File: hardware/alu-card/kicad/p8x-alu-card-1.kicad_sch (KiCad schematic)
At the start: 9 parts, among them U1 74HCT377, U2 74HCT244, U3 74HCT377, U4 74HCT244, U5 74HCT377, U6 74HCT244, U7 74HCT377, U8 74HCT244, U9 74HCT181

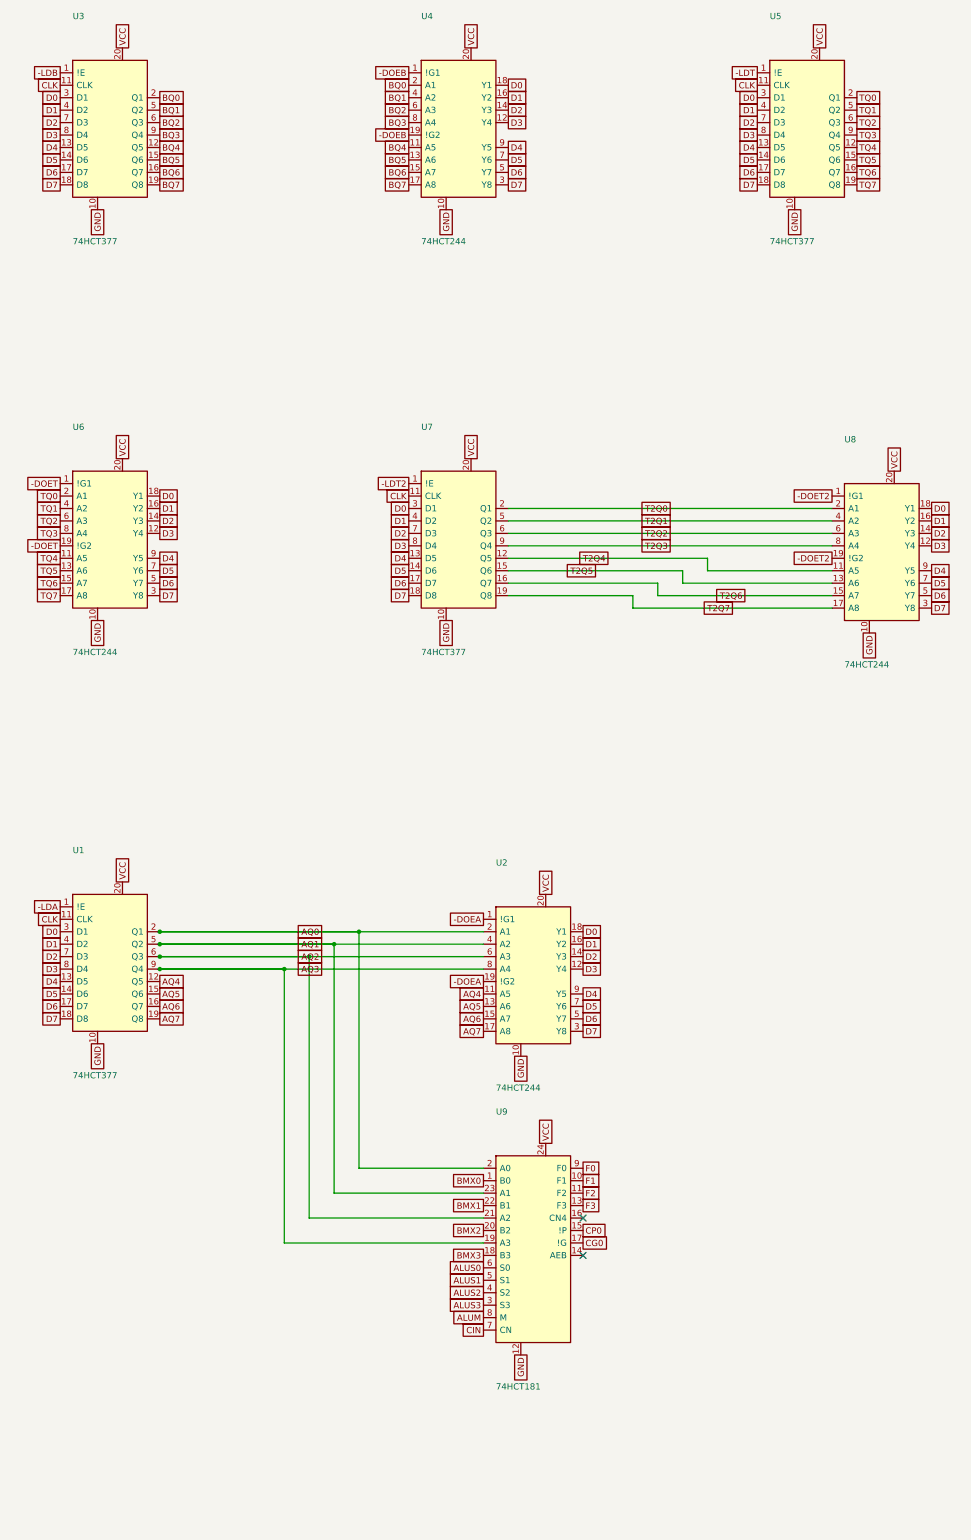
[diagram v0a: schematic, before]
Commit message: feat(sch): draw every P8X card schematic by function
Extend the functional-sheet grouping from the io-card to the control,
regbank, alu, memory, cf, ps2 and bustest cards. functional_sheets now
attaches unnamed glue gates, LEDs, resistors and connectors to the block
they share the most local nets with, so each block lists only its main
parts. A net with two or more pins on a sheet is now wired there even if
it continues elsewhere (its global name label rides on the wire), and
every wire is oriented by drawing side. The regbank gets one pointer per
sheet; the ps2 latches share a sheet with the AVR so the mailbox bus is
drawn. The bustest probe resistors use a straight-order RNISO8DSTR
drawing (the reversed B side forced every wire to cross and the sheet
fell back to labels). build_sch.sh now shows ELK fallbacks and clears old
numbered sheets before a build. All eight netlists match the boards,
ERC 0 errors; the boards change only in footprint link paths.

Co-Authored-By: Claude Opus 5.5 <noreply@anthropic.com>
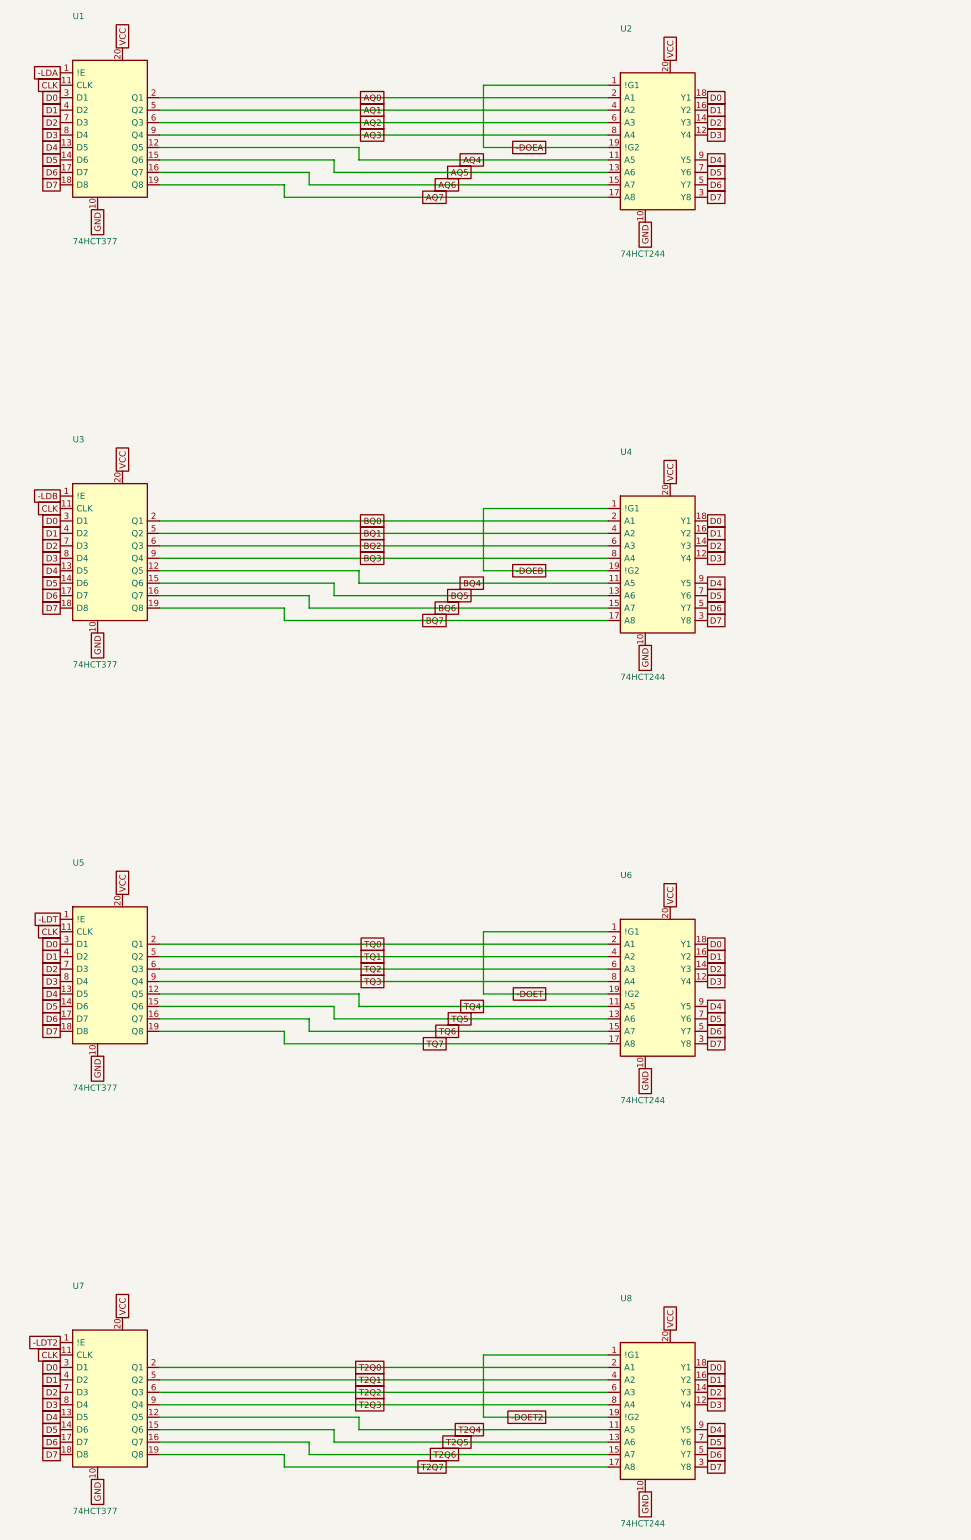
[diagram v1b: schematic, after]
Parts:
- removed U9: 74HCT181, Package_DIP:DIP-24_W15.24mm, symbol p8x:74181
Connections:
- no-connect marks 2 -> 0
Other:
- moved on the sheet: U1, U2, U3, U4, U5, U6, U7, U8
